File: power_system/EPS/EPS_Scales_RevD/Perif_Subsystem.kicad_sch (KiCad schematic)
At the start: 45 parts, among them CN1 DF11-16DP-2DSA(08), U12 TPS1HB08BQPWPRQ1, U13 LT8612EUDE#PBF, U16 INA260AIPWR

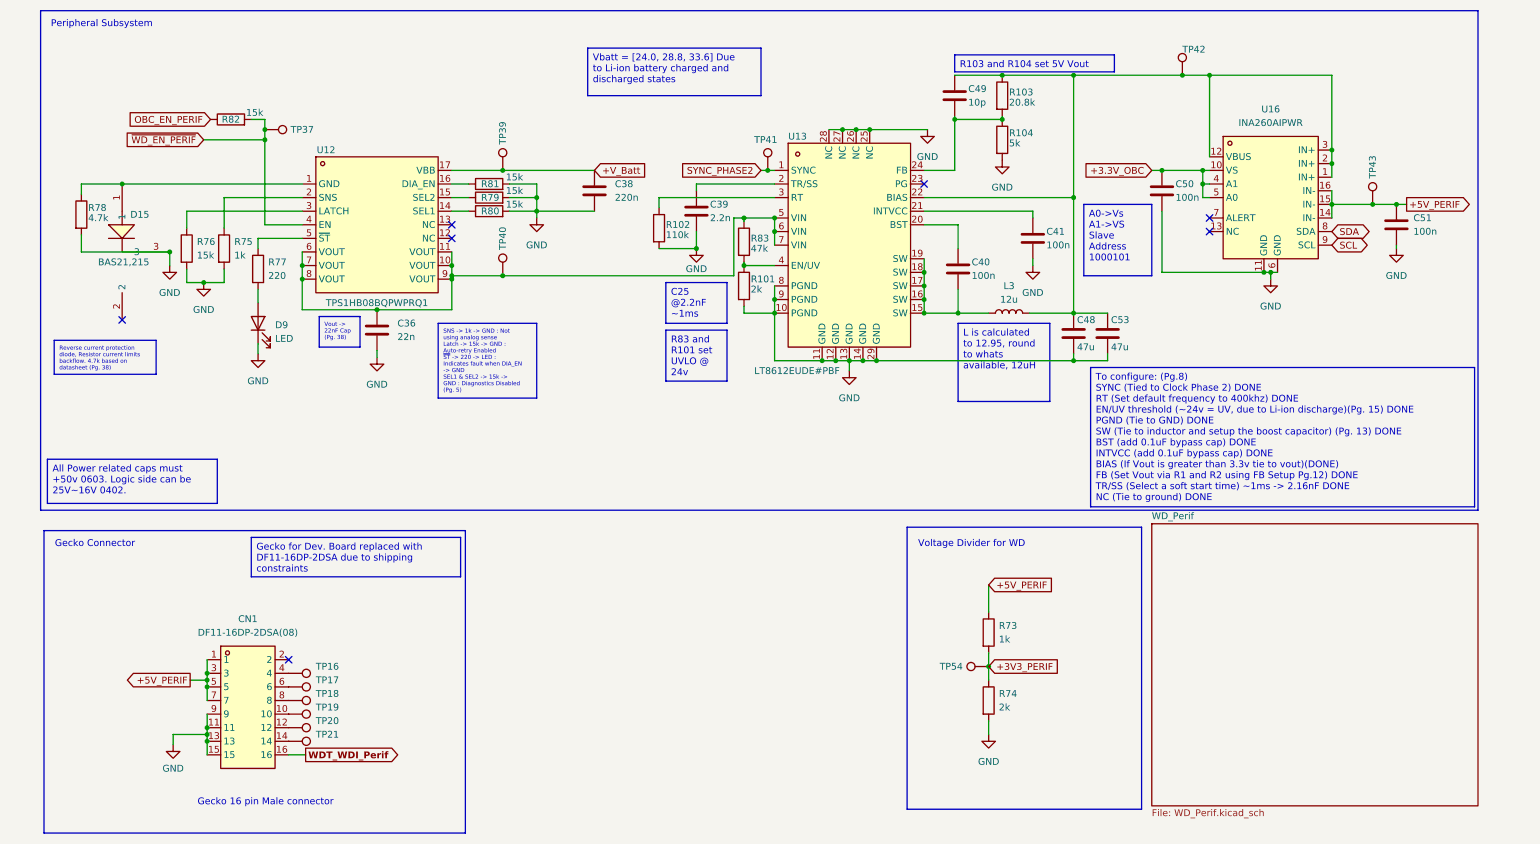
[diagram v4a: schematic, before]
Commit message: Schematic and PCB Cleanup
After a fairly eventful review with Andrew it is time for some schematic cleanup, PCB cleanup and a well earned break. Tomorrow my goal is to knock out the full Schematic Cleanup, which im almost done with, I just need to redo the jetson portion and then im done. And then for the PCB, theres some minor things like removing components that were removed in the schematic, adding more vias, and then changing some fill parameters. After that I need to do the BOM and the production files. John and I will order the boards tomorrow (HOPEFULLY)
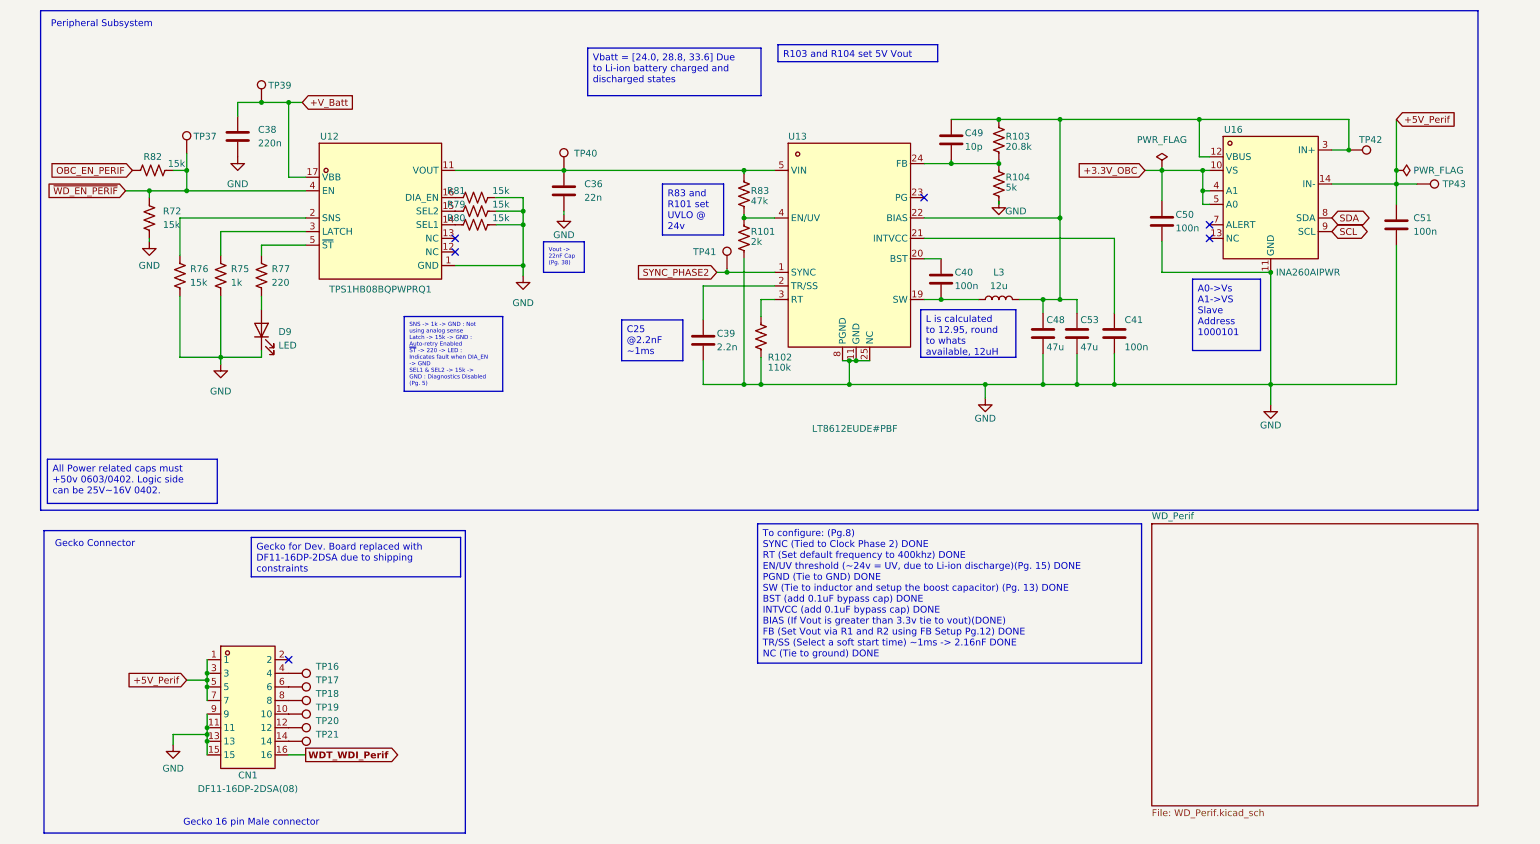
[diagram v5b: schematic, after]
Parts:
- removed D15: BAS21,215, EPS:SOT-23-3_L2.9-W1.6-P1.90-LS2.8-BR, symbol EPS:BAS21,215
- removed R73: 1k, EPS:R0402, symbol Device:R
- removed R74: 2k, EPS:R0402, symbol Device:R
- removed R78: 4.7k, EPS:R0402, symbol Device:R
- removed TP54: TestPoint, TestPoint:TestPoint_Pad_1.0x1.0mm, symbol Connector:TestPoint
- added R72: 15k, EPS:R0402, symbol Device:R_US
- R101, R102, R103, R104, R75, R76, R77, R79, R80, R81, R82, R83: symbol Device:R -> Device:R_US
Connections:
- net GND: now also U12.1 (GND), R72.2; no longer U13.10 (PGND), U13.26 (NC), U13.27 (NC), U13.28 (NC), U13.29 (GND), U13.9 (PGND), U16.6 (GND)
- net ~{WD_EN_PERIF}: now also R72.1
- net at C48.1, C49.1, C53.1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: no longer U16.1 (IN+), U16.2 (IN+)
- net at C40.2, L3.1, U13.16 (SW)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: no longer U13.15 (SW), U13.17 (SW), U13.18 (SW)
- net at U12.12 (NC): now also U12.9 (VOUT)
- net at U12.13 (NC): now also U12.10 (VOUT)
- net at U12.2 (SNS): now also R76.1; no longer R75.1
- net at U12.3 (LATCH): now also R75.1; no longer R76.1
- net +5V_PERIF renamed +5V_Perif
- net +5V_Perif: no longer U16.15 (IN-), U16.16 (IN-)
- new net: C36.1, R83.1, TP40.1, U12.11 (VOUT), U13.5 (VIN)
- now unconnected: U12.6 (VOUT), U12.7 (VOUT), U12.8 (VOUT), U13.6 (VIN), U13.7 (VIN)
- no-connect marks 7 -> 6
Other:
- note removed: "Voltage Divider for WD"
- moved on the sheet: C36, C38, C39, C40, C41, C48, C49, C50, C53, D9, L3, TP37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

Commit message: Big Changes
Schematic legibility overhaul
Symbols have had pin numbers reduced to have easier legibility, the footprints have had pins renamed to the same pin numbers because pin hiding doesnt work yet in Kicad, grrr.

Some redundancies were removed and the layout was cleaned up as well.
The correct xt-60 symbol was added and I fixed the pin numbering as well.
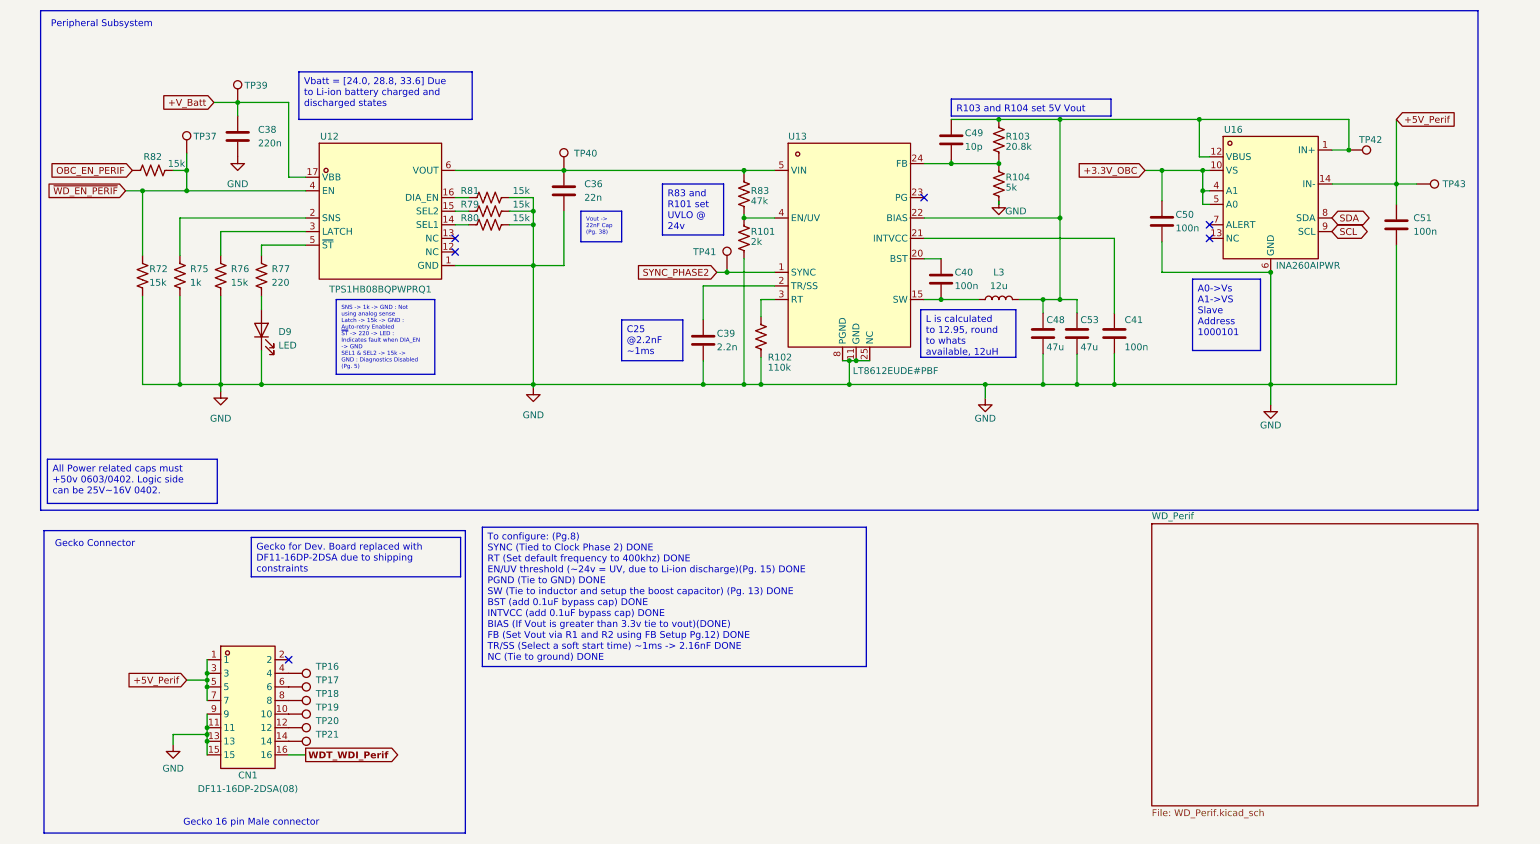
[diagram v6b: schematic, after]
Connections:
- net GND: now also U16.6 (GND); no longer U13.12 (GND), U13.13 (GND), U13.14 (GND), U16.11 (GND)
- net at C48.1, C49.1, C53.1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: now also U16.1 (IN+); no longer U16.3 (IN+)
- net at U13.15 (SW): now also C40.2, L3.1
- net at C36.1, R83.1, TP40.1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: now also U12.6 (VOUT); no longer U12.11 (VOUT)
- net at U12.13 (NC): no longer U12.10 (VOUT)
- net at U12.12 (NC): no longer U12.9 (VOUT)
- net at U12.2 (SNS): now also R75.1; no longer R76.1
- net at U12.3 (LATCH): now also R76.1; no longer R75.1
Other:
- moved on the sheet: R72, R75, R76, R79, R80, R81, TP39
